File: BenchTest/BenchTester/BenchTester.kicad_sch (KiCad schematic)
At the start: 41 parts, among them J1 Conn_01x01_Socket, J2 Conn_01x01_Socket, J3 Conn_01x01_Socket, J4 Conn_01x02_Socket, J5 Conn_01x01_Socket, J6 Conn_01x01_Socket, J7 Conn_01x01_Socket, J8 Conn_01x01_Socket, J9 Conn_01x01_Socket, Q1 Q_NMOS_GDS, Q2 Q_NMOS_GDS, Q3 Q_NMOS_GDS, Q5 Q_NMOS_GDS

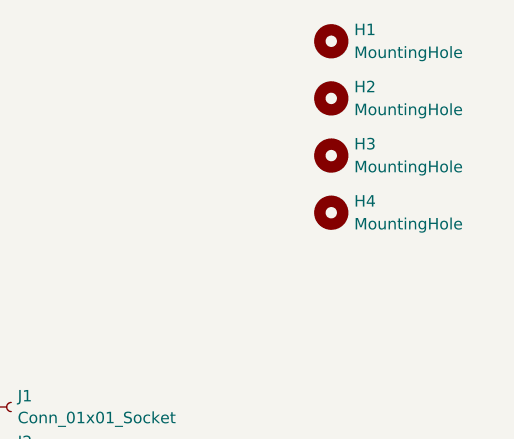
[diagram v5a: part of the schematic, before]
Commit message: Re-placement of positions to reduce trace length
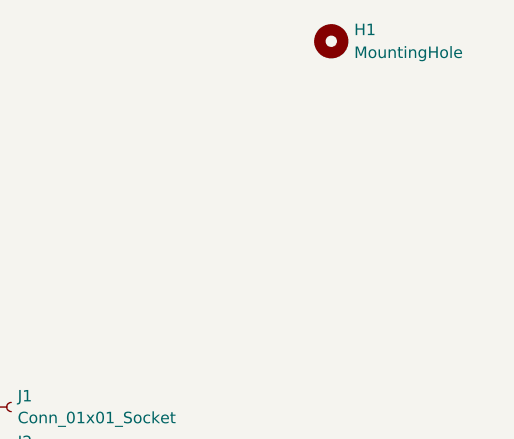
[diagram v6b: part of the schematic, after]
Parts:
- removed H2, H3, H4: MountingHole, MountingHole:MountingHole_3.2mm_M3, symbol Mechanical:MountingHole
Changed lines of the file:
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@@
-	)
-	(symbol
-		(lib_id "Mechanical:MountingHole")
-		(at 260.35 35.56 0)
-		(unit 1)
-		(exclude_from_sim yes)
-		(in_bom no)
-		(on_board yes)
-		(dnp no)
-		(fields_autoplaced yes)
-		(property "Reference" "H4"
-			(at 262.89 34.2899 0)
-			(effects
-				(font
-					(size 1.27 1.27)
-				)
-				(justify left)
-			)
-		)
-		(property "Value" "MountingHole"
-			(at 262.89 36.8299 0)
-			(effects
-				(font
-					(size 1.27 1.27)
-				)
-				(justify left)
-			)
-		)
-		(property "Footprint" "MountingHole:MountingHole_3.2mm_M3"
-			(at 260.35 35.56 0)
-			(effects
-				(font
-					(size 1.27 1.27)
-				)
-				(hide yes)
-			)
-		)
-		(property "Datasheet" "~"
-			(at 260.35 35.56 0)
-			(effects
-				(font
-					(size 1.27 1.27)
-				)
-				(hide yes)
-			)
-		)
-		(property "Description" "Mounting Hole without connection"
-			(at 260.35 35.56 0)
-			(effects
-				(font
-					(size 1.27 1.27)
-				)
-				(hide yes)
-			)
-		)
-		(instances
-			(project "BenchTester"
-				(path "/4803142b-5151-422b-a498-ba37418ce51c"
-					(reference "H4")
-					(unit 1)
-				)
-			)
-		)
-	)
-	(symbol
-		(lib_id "Mechanical:MountingHole")
-		(at 260.35 22.86 0)
-		(unit 1)
-		(exclude_from_sim yes)
-		(in_bom no)
-		(on_board yes)
-		(dnp no)
-		(fields_autoplaced yes)
-		(property "Reference" "H2"
-			(at 262.89 21.5899 0)
-			(effects
-				(font
-					(size 1.27 1.27)
-				)
-				(justify left)
-			)
-		)
-		(property "Value" "MountingHole"
-			(at 262.89 24.1299 0)
-			(effects
-				(font
-					(size 1.27 1.27)
-				)
-				(justify left)
-			)
-		)
-		(property "Footprint" "MountingHole:MountingHole_3.2mm_M3"
-			(at 260.35 22.86 0)
-			(effects
-				(font
-					(size 1.27 1.27)
-				)
-				(hide yes)
-			)
-		)
-		(property "Datasheet" "~"
-			(at 260.35 22.86 0)
-			(effects
-				(font
-					(size 1.27 1.27)
-				)
-				(hide yes)
-			)
-		)
-		(property "Description" "Mounting Hole without connection"
-			(at 260.35 22.86 0)
-			(effects
-				(font
-					(size 1.27 1.27)
-				)
-				(hide yes)
-			)
-		)
-		(instances
-			(project "BenchTester"
-				(path "/4803142b-5151-422b-a498-ba37418ce51c"
-					(reference "H2")
-					(unit 1)
-				)
-			)
-		)
 	)
 	(symbol
@@
 					(unit 1)
 				)
-			)
-		)
-	)
-	(symbol
-		(lib_id "Mechanical:MountingHole")
-		(at 260.35 29.21 0)
-		(unit 1)
-		(exclude_from_sim yes)
-		(in_bom no)
-		(on_board yes)
-		(dnp no)
-		(fields_autoplaced yes)
-		(property "Reference" "H3"
-			(at 262.89 27.9399 0)
-			(effects
-				(font
-					(size 1.27 1.27)
-				)
-				(justify left)
-			)
-		)
-		(property "Value" "MountingHole"
-			(at 262.89 30.4799 0)
-			(effects
-				(font
-					(size 1.27 1.27)
-				)
-				(justify left)
-			)
-		)
-		(property "Footprint" "MountingHole:MountingHole_3.2mm_M3"
-			(at 260.35 29.21 0)
-			(effects
-				(font
-					(size 1.27 1.27)
-				)
-				(hide yes)
-			)
-		)
-		(property "Datasheet" "~"
-			(at 260.35 29.21 0)
-			(effects
-				(font
-					(size 1.27 1.27)
-				)
-				(hide yes)
-			)
-		)
-		(property "Description" "Mounting Hole without connection"
-			(at 260.35 29.21 0)
-			(effects
-				(font
-					(size 1.27 1.27)
-				)
-				(hide yes)
-			)
-		)
-		(instances
-			(project "BenchTester"
-				(path "/4803142b-5151-422b-a498-ba37418ce51c"
-					(reference "H3")
-					(unit 1)
-				)
